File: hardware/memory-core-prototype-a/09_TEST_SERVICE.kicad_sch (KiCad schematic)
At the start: 1 part, among them J909 SHEET_INTERFACE_NOT_FITTED

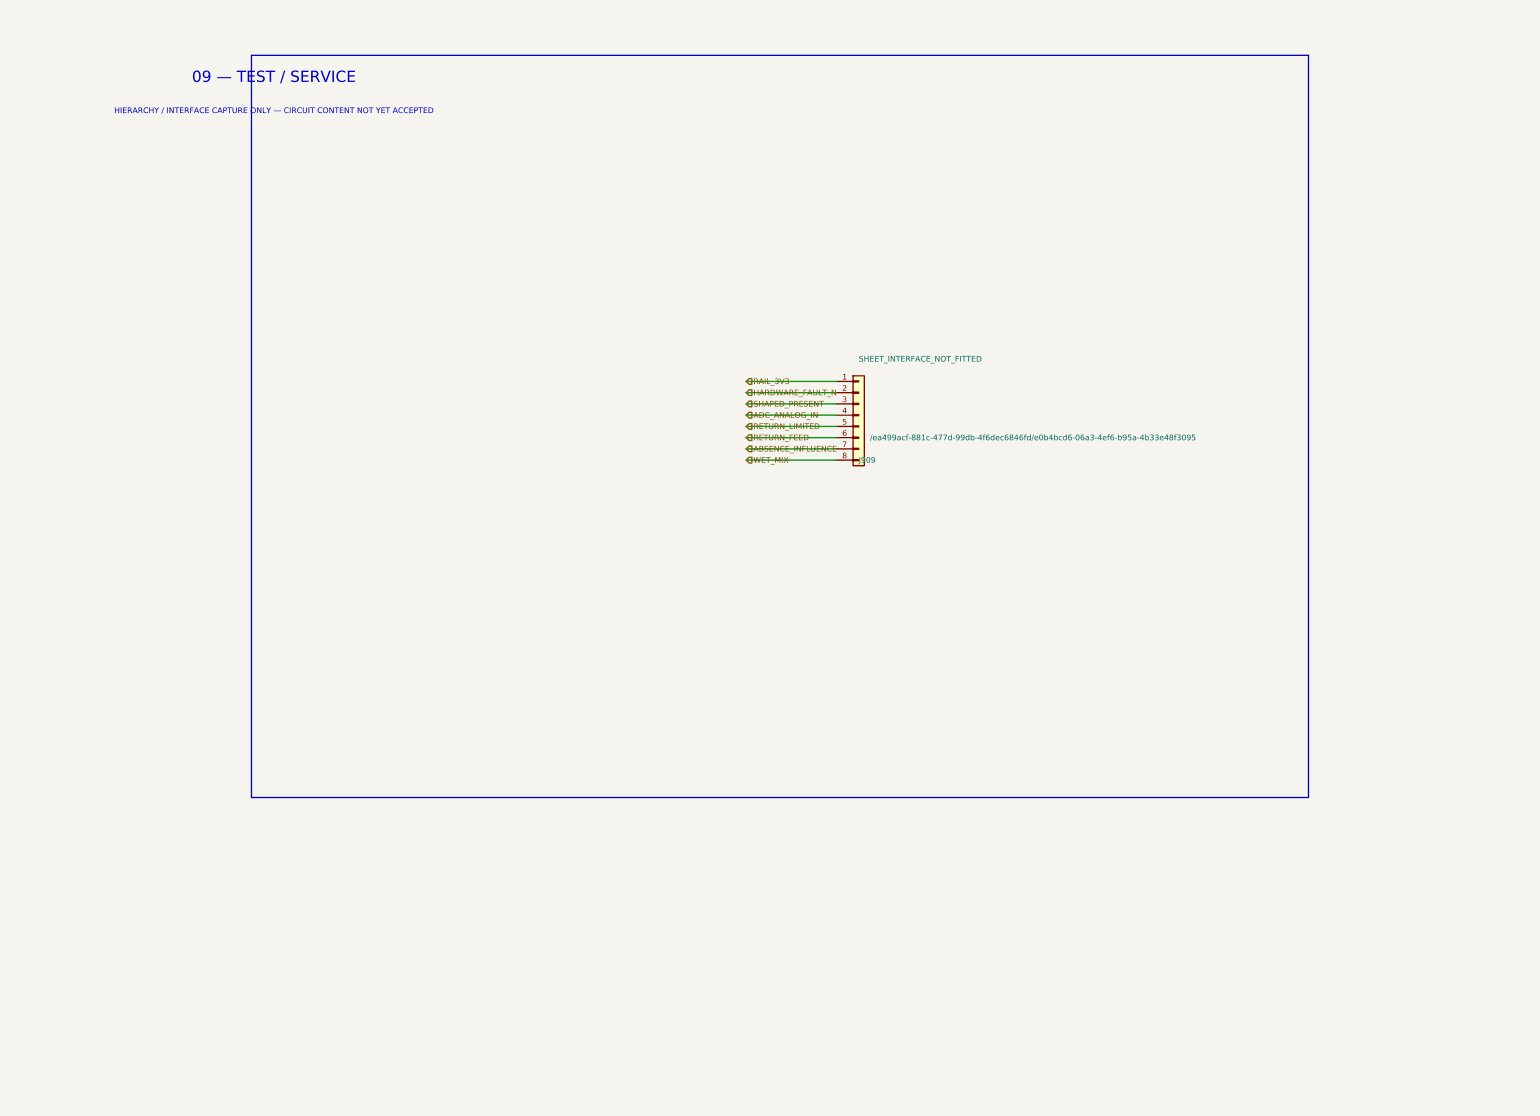
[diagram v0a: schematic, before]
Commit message: Capture ERC-validated test service sheet
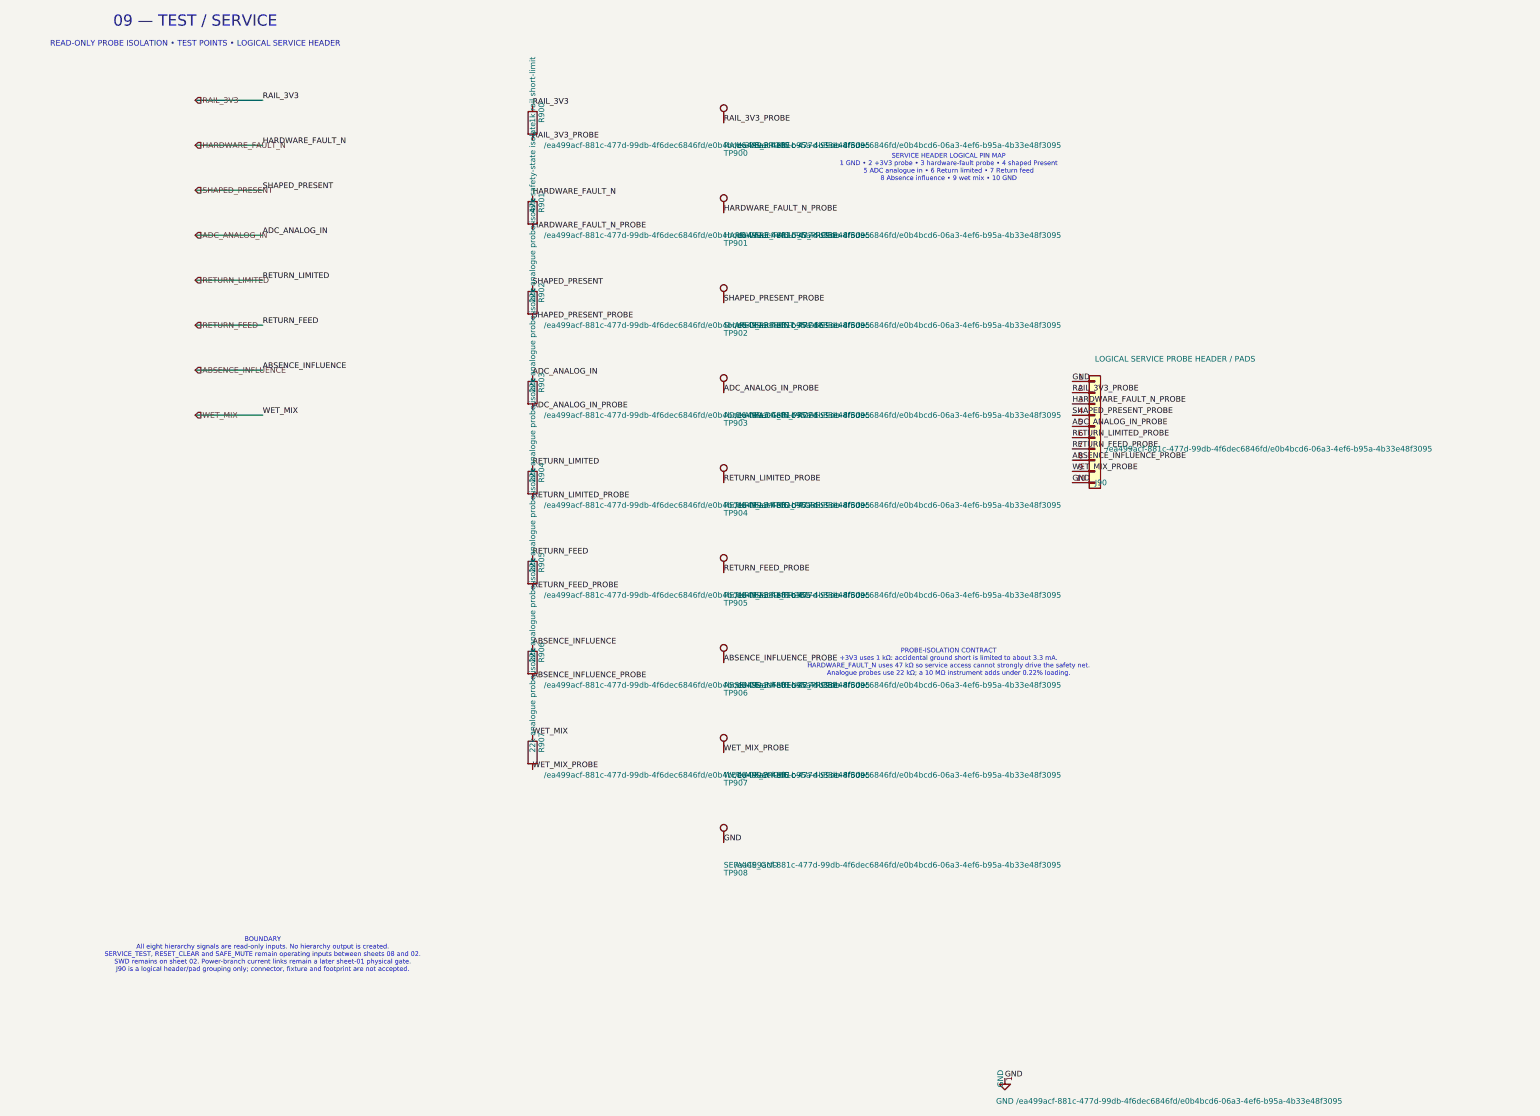
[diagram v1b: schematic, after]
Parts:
- removed J909: SHEET_INTERFACE_NOT_FITTED, symbol Connector_Generic:Conn_01x08
- added J90: LOGICAL SERVICE PROBE HEADER / PADS, symbol Connector_Generic:Conn_01x10
- added R900: 1k rail short-limit, Resistor_SMD:R_0805_2012Metric, symbol Device:R
- added R901: 47k safety-state isolate, Resistor_SMD:R_0805_2012Metric, symbol Device:R
- added R902, R903, R904, R905, R906, R907: 22k analogue probe isolate, Resistor_SMD:R_0805_2012Metric, symbol Device:R
- added TP900: RAIL_3V3_PROBE, symbol Connector:TestPoint
- added TP901: HARDWARE_FAULT_N_PROBE, symbol Connector:TestPoint
- added TP902: SHAPED_PRESENT_PROBE, symbol Connector:TestPoint
- added TP903: ADC_ANALOG_IN_PROBE, symbol Connector:TestPoint
- added TP904: RETURN_LIMITED_PROBE, symbol Connector:TestPoint
- added TP905: RETURN_FEED_PROBE, symbol Connector:TestPoint
- added TP906: ABSENCE_INFLUENCE_PROBE, symbol Connector:TestPoint
- added TP907: WET_MIX_PROBE, symbol Connector:TestPoint
- added TP908: SERVICE_GND, symbol Connector:TestPoint
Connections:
- net ABSENCE_INFLUENCE: now also R906.1
- net ADC_ANALOG_IN: now also R903.1
- net HARDWARE_FAULT_N: now also R901.1
- net RAIL_3V3: now also R900.1
- net RETURN_FEED: now also R905.1
- net RETURN_LIMITED: now also R904.1
- net SHAPED_PRESENT: now also R902.1
- net WET_MIX: now also R907.1
- new net ABSENCE_INFLUENCE_PROBE: J90.8 (Pin_8), R906.2, TP906.1
- new net ADC_ANALOG_IN_PROBE: J90.5 (Pin_5), R903.2, TP903.1
- new net GND: J90.1 (Pin_1), J90.10 (Pin_10), TP908.1
- new net HARDWARE_FAULT_N_PROBE: J90.3 (Pin_3), R901.2, TP901.1
- new net RAIL_3V3_PROBE: J90.2 (Pin_2), R900.2, TP900.1
- new net RETURN_FEED_PROBE: J90.7 (Pin_7), R905.2, TP905.1
- new net RETURN_LIMITED_PROBE: J90.6 (Pin_6), R904.2, TP904.1
- new net SHAPED_PRESENT_PROBE: J90.4 (Pin_4), R902.2, TP902.1
- new net WET_MIX_PROBE: J90.9 (Pin_9), R907.2, TP907.1
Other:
- note added: "BOUNDARY All eight hierarchy signals are read-only inputs. No hierarchy output is created. SERVICE_TEST, RESET_CLEAR and SAFE_MUTE remain operating inputs between sheets 08 and 02. SWD remains on sheet 02. Power-branch current links remain a later sheet-01 physical gate. J90 is a logical header/pad grouping only; connector, fixture and footprint are not accepted."
- note added: "PROBE-ISOLATION CONTRACT +3V3 uses 1 kΩ: accidental ground short is limited to about 3.3 mA. HARDWARE_FAULT_N uses 47 kΩ so service access cannot strongly drive the safety net. Analogue probes use 22 kΩ; a 10 MΩ instrument adds under 0.22% loading."
- note added: "READ-ONLY PROBE ISOLATION • TEST POINTS • LOGICAL SERVICE HEADER"
- note added: "SERVICE HEADER LOGICAL PIN MAP 1 GND • 2 +3V3 probe • 3 hardware-fault probe • 4 shaped Present 5 ADC analogue in • 6 Return limited • 7 Return feed 8 Absence influence • 9 wet mix • 10 GND"
- note removed: "HIERARCHY / INTERFACE CAPTURE ONLY — CIRCUIT CONTENT NOT YET ACCEPTED"
- title: Memory Core Prototype A — TEST / SERVICE -> Memory Core Prototype A — Test / Service
